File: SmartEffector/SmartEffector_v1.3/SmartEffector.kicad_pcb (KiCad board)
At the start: 2 copper layers, 83.2 x 72.1 mm, 53 parts, among them M1 FID, M10 M_2.9mm, M11 M_2.9mm, M13 Ziptie, M15 OSHW_Logo, M16 12mm, M2 FID, M3 M_2.9mm, M4 M_2.9mm, M5 M_2.9mm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

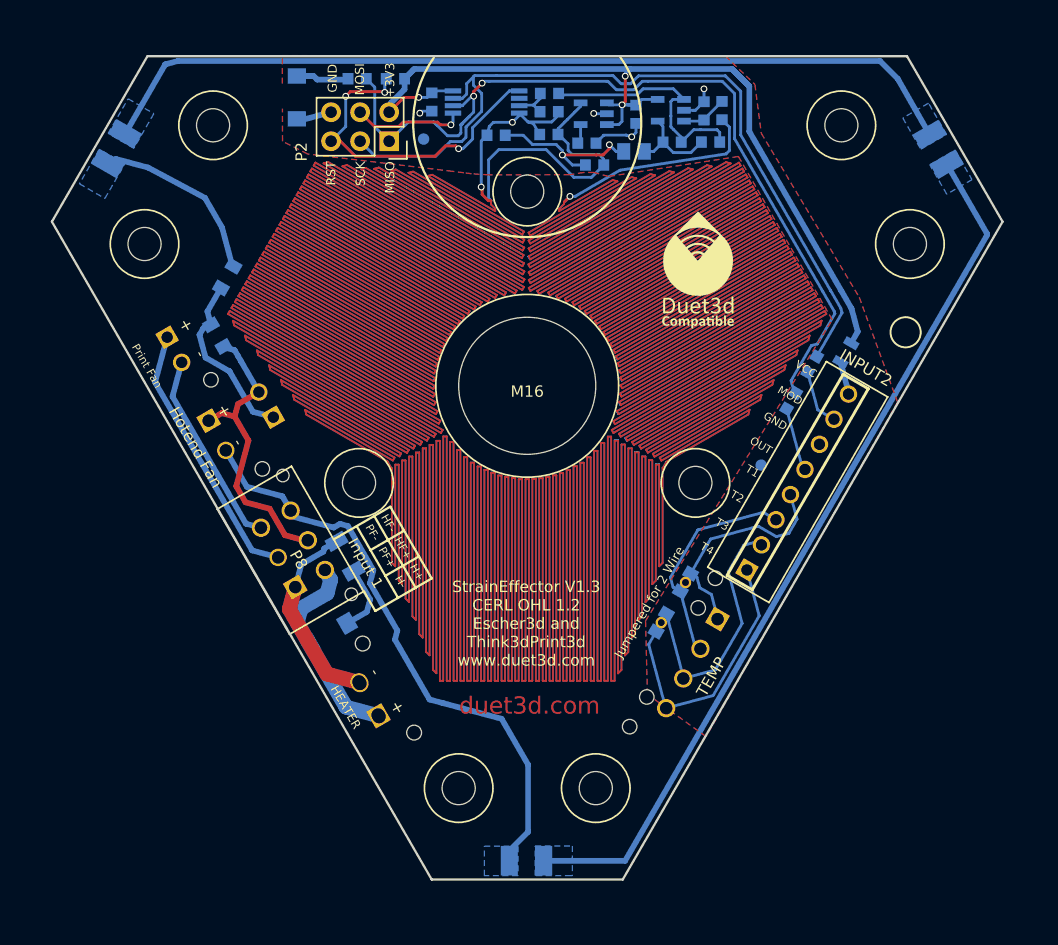
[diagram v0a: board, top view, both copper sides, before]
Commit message: Added modifications for puplomaker delta printer
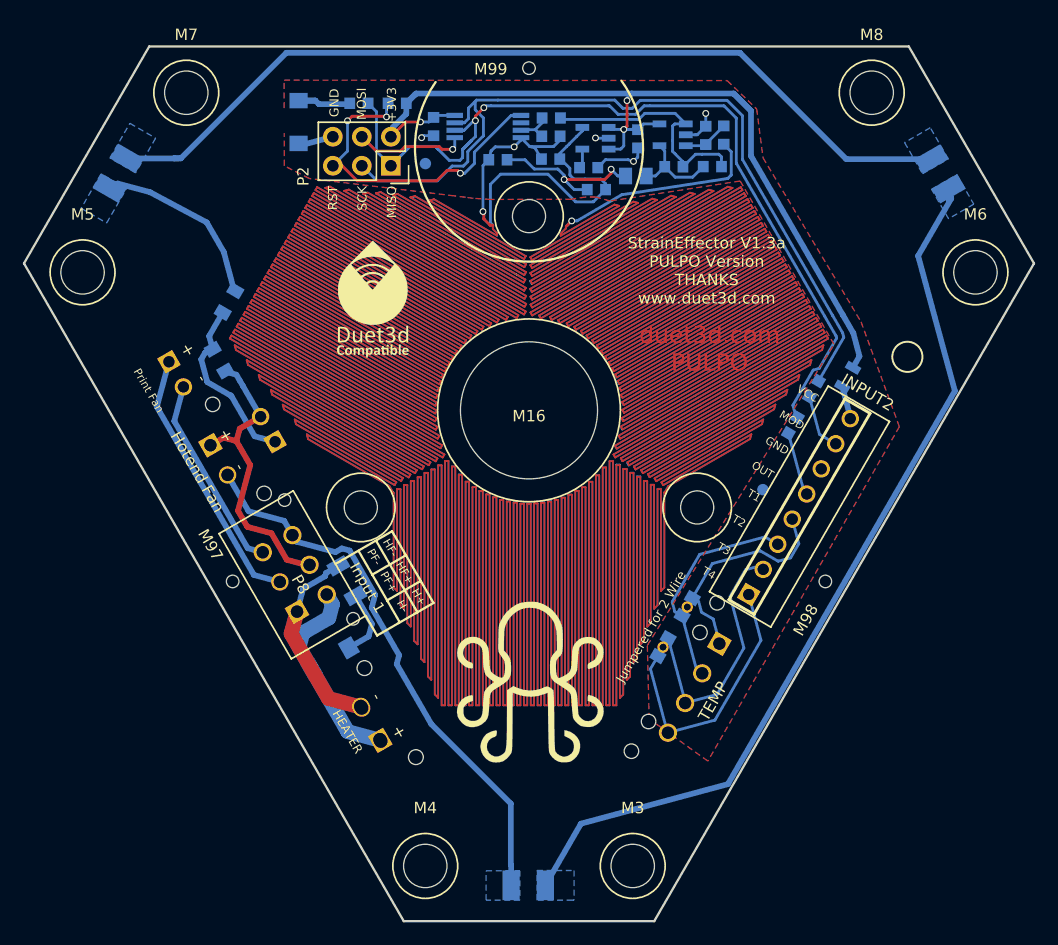
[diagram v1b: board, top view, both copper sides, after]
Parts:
- added G99: LOGO, Wire_Pads:LOGO, F.Cu at (84.2, 149.5)
- added M97: M2_1.4mm, Wire_Pads:M2_2.4, F.Cu at (58.2, 140.9)
- added M98: M2_1.4mm, Wire_Pads:M2_2.4, F.Cu at (110.1, 140.9)
- added M99: M2_1.4mm, Wire_Pads:M2_2.4, F.Cu at (84.2, 96.0)
- M3, M4, M5, M6, M7, M8: value M_2.9mm -> M_3.8mm; footprint complib:MountingHole_2.9mm -> Wire_Pads:M4_3.8
- moved M15 28.6 mm to (70.5, 116.1)
- moved M3 7.54 mm to (93.3, 165.8)
- moved M4 7.41 mm to (75.1, 165.8)
- moved M6 6.25 mm to (123.3, 113.8)
- moved M5 5.97 mm to (45.1, 113.8)
- moved M8 3.90 mm to (114.2, 98.1)
- moved M7 3.69 mm to (54.2, 98.1)
- moved D3 2.15 mm to (64.0, 100.7)
- moved M13 2.15 mm to (117.3, 121.2)
- moved P9 2.15 mm to (57.1, 130.3)
- moved C8 2.15 mm to (99.7, 101.8)
- moved R1 2.15 mm to (100.2, 104.6)
- moved R7 2.15 mm to (72.6, 99.0)
- moved R14 2.15 mm to (81.5, 104.0)
- moved JP3 2.15 mm to (61.3, 127.6)
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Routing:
- net H_Fan_-: track 51.5 -> 49.1 mm
- net Net-(D7-Pad2): track 77.2 -> 79.2 mm
- net Net-(D1-Pad1): track 77.1 -> 78.5 mm
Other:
- board size 83.2 x 72.1 mm -> 88.4 x 76.6 mm
- board text added: "StrainEffector V1.3a PULPO Version THANKS www.duet3d.com"
- board text added: "duet3d.com PULPO"
- board text removed: "StrainEffector V1.3 CERL OHL 1.2 Escher3d and Think3dPrint3d www.duet3d.com"
- board text removed: "duet3d.com"

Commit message: charlio modification, gerbers and autogenerated BOM list
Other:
- board size 88.4 x 76.6 mm -> 86.9 x 76.6 mm
- board text added: "Based on StrainEffector V1.3a www.duet3d.com Pulpomaker Version"
- board text added: "David Carlos Sergio Santi Raúl Xavi Oriol Victor Javier"
- board text added: "Jumpered for 2 wire"
- board text removed: "Jumpered for 2 Wire"
- board text removed: "StrainEffector V1.3a PULPO Version THANKS www.duet3d.com"
- board text removed: "duet3d.com PULPO"
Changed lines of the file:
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@@
-(kicad_pcb (version 20171130) (host pcbnew 5.0.0+dfsg1-2)
+(kicad_pcb (version 20171130) (host pcbnew "(5.0.0)")
   (general
     (thickness 1.6)
-    (drawings 77)
+    (drawings 82)
     (tracks 1429)
     (zones 0)
@@
     (0 F.Cu signal)
     (31 B.Cu signal)
-    (32 B.Adhes user)
-    (33 F.Adhes user)
-    (34 B.Paste user)
-    (35 F.Paste user)
+    (32 B.Adhes user hide)
+    (33 F.Adhes user hide)
+    (34 B.Paste user hide)
+    (35 F.Paste user hide)
     (36 B.SilkS user)
     (37 F.SilkS user)
     (38 B.Mask user)
     (39 F.Mask user)
-    (40 Dwgs.User user)
-    (41 Cmts.User user)
-    (42 Eco1.User user)
-    (43 Eco2.User user)
+    (40 Dwgs.User user hide)
+    (41 Cmts.User user hide)
+    (42 Eco1.User user hide)
+    (43 Eco2.User user hide)
     (44 Edge.Cuts user)
-    (45 Margin user)
-    (46 B.CrtYd user)
-    (47 F.CrtYd user)
-    (48 B.Fab user)
-    (49 F.Fab user)
+    (45 Margin user hide)
+    (46 B.CrtYd user hide)
+    (47 F.CrtYd user hide)
+    (48 B.Fab user hide)
+    (49 F.Fab user hide)
   )
   (setup
@@
   (module Wire_Pads:M4_3.8 locked (layer F.Cu)
     (at 45.106803 113.838022)
-    (fp_text reference M5 (at 0 -5.08) (layer F.SilkS)
+    (fp_text reference M5 (at 0 -5.08) (layer F.SilkS) hide
       (effects (font (size 1 1) (thickness 0.15)))
     )
@@
   (module Wire_Pads:M4_3.8 locked (layer F.Cu)
     (at 54.186944 98.110756)
-    (fp_text reference M7 (at 0 -5.08) (layer F.SilkS)
+    (fp_text reference M7 (at 4.302525 -2.218279) (layer F.SilkS) hide
       (effects (font (size 1 1) (thickness 0.15)))
     )
@@
   (module Wire_Pads:M4_3.8 (layer F.Cu)
     (at 114.186946 98.110757)
-    (fp_text reference M8 (at 0 -5.08) (layer F.SilkS)
+    (fp_text reference M8 (at -3.881477 -1.83728) (layer F.SilkS) hide
       (effects (font (size 1 1) (thickness 0.15)))
     )
@@
   (module Wire_Pads:M4_3.8 locked (layer F.Cu)
     (at 123.267079 113.83802)
-    (fp_text reference M6 (at 0 -5.08) (layer F.SilkS)
+    (fp_text reference M6 (at 1.38939 -3.721543) (layer F.SilkS) hide
       (effects (font (size 1 1) (thickness 0.15)))
     )
@@
   (module Wire_Pads:M4_3.8 locked (layer F.Cu)
     (at 93.267087 165.799547)
-    (fp_text reference M3 (at 0 -5.08) (layer F.SilkS)
+    (fp_text reference M3 (at 0 -5.08) (layer F.SilkS) hide
       (effects (font (size 1 1) (thickness 0.15)))
     )
@@
   (module Wire_Pads:M4_3.8 locked (layer F.Cu)
     (at 75.106796 165.799547)
-    (fp_text reference M4 (at 0 -5.08) (layer F.SilkS)
+    (fp_text reference M4 (at 0 -5.08) (layer F.SilkS) hide
       (effects (font (size 1 1) (thickness 0.15)))
     )
@@
   (module Wire_Pads:M2_2.4 (layer F.Cu)
     (at 84.186943 95.960759)
-    (fp_text reference M99 (at -3.348806 0.084343) (layer F.SilkS)
+    (fp_text reference M99 (at -3.348806 0.084343) (layer F.SilkS) hide
       (effects (font (size 1 1) (thickness 0.15)))
     )
@@
   (module Wire_Pads:M2_2.4 (layer F.Cu)
     (at 58.244843 140.893787 120)
-    (fp_text reference M97 (at 3.736499 -0.083013 120) (layer F.SilkS)
+    (fp_text reference M97 (at 3.736499 -0.083013 120) (layer F.SilkS) hide
       (effects (font (size 1 1) (thickness 0.15)))
     )
@@
   (module Wire_Pads:M2_2.4 (layer F.Cu)
     (at 110.129047 140.893789 240)
-    (fp_text reference M98 (at 3.777945 -0.201285 240) (layer F.SilkS)
+    (fp_text reference M98 (at 3.777945 -0.201285 240) (layer F.SilkS) hide
       (effects (font (size 1 1) (thickness 0.15)))
     )
@@
       (effects (font (size 1 1) (thickness 0.15)) (justify mirror))
     )
-    (fp_text user K (at -3.957066 0.991181 240) (layer B.SilkS)
+    (fp_text user K (at -3.957066 0.991181 240) (layer B.SilkS) hide
       (effects (font (size 0.9 0.9) (thickness 0.1)) (justify mirror))
     )
@@
       (effects (font (size 1 1) (thickness 0.15)) (justify mirror))
     )
-    (fp_text user K (at -4.102768 0.812217) (layer B.SilkS)
+    (fp_text user K (at -4.102768 0.812217) (layer B.SilkS) hide
       (effects (font (size 0.9 0.9) (thickness 0.1)) (justify mirror))
     )
@@
       (effects (font (size 1 1) (thickness 0.15)) (justify mirror))
     )
-    (fp_text user K (at -3.41469 0.797969 120) (layer B.SilkS)
+    (fp_text user K (at -3.41469 0.797969 120) (layer B.SilkS) hide
       (effects (font (size 0.9 0.9) (thickness 0.1)) (justify mirror))
     )
@@
       (xy -1.056581 0.682429)) (layer F.SilkS) (width 0.01))
   )
+  (gr_line (start 126.959844 115.486448) (end 96.601596 168.068477) (layer Edge.Cuts) (width 0.2))
+  (gr_arc (start 53.839971 99.003171) (end 53.839971 94.003171) (angle -60) (layer Edge.Cuts) (width 0.2))
+  (gr_arc (start 45.766723 112.986448) (end 41.436596 110.486448) (angle -60) (layer Edge.Cuts) (width 0.2))
+  (gr_line (start 53.839971 94.003171) (end 114.556469 94.003171) (layer Edge.Cuts) (width 0.2))
+  (gr_arc (start 114.556469 99.003171) (end 118.886596 96.503171) (angle -60) (layer Edge.Cuts) (width 0.2))
+  (gr_line (start 118.886596 96.503171) (end 126.959844 110.486448) (layer Edge.Cuts) (width 0.2))
+  (gr_arc (start 122.629717 112.986448) (end 126.959844 115.486448) (angle -60) (layer Edge.Cuts) (width 0.2))
+  (gr_arc (start 92.271469 165.568477) (end 92.271469 170.568477) (angle -60) (layer Edge.Cuts) (width 0.2))
+  (gr_arc (start 76.124971 165.568477) (end 71.794844 168.068477) (angle -60) (layer Edge.Cuts) (width 0.2))
+  (gr_line (start 71.794844 168.068477) (end 41.436596 115.486448) (layer Edge.Cuts) (width 0.2))
+  (gr_line (start 41.436596 110.486448) (end 49.509844 96.503171) (layer Edge.Cuts) (width 0.2))
+  (gr_line (start 92.271469 170.568477) (end 76.124971 170.568477) (layer Edge.Cuts) (width 0.2))
   (gr_text T2 (at 102.562039 135.614841 -30) (layer F.SilkS)
     (effects (font (size 0.7 0.7) (thickness 0.08)))
@@
   )
   (gr_arc (start 84.186942 102.916111) (end 92.272014 97.055601) (angle 251) (layer F.SilkS) (width 0.2))
-  (gr_text "Jumpered for 2 Wire" (at 94.875525 144.858812 60) (layer F.SilkS)
+  (gr_text "Jumpered for 2 wire" (at 95.192469 144.533477 60) (layer F.SilkS)
     (effects (font (size 0.8 0.8) (thickness 0.1)))
   )
@@
     (effects (font (size 0.8 0.8) (thickness 0.1)) (justify right))
   )
-  (gr_text "duet3d.com\nPULPO" (at 99.994702 120.529389) (layer F.Mask)
-    (effects (font (size 1.5 1.5) (thickness 0.26)))
-  )
-  (gr_text "duet3d.com\nPULPO" (at 99.997469 120.530477) (layer F.Cu)
-    (effects (font (size 1.5 1.5) (thickness 0.3)))
+  (gr_text "David\nCarlos\nSergio\nSanti\nRaúl\nXavi\nOriol\nVictor\nJavier" (at 98.367469 118.879477) (layer Dwgs.User)
+    (effects (font (size 1.5 1.5) (thickness 0.26)) (justify mirror))
   )
   (gr_text "RST\n\nSCK\n\nMISO" (at 69.593453 106.259225 90) (layer F.SilkS)
@@
     (effects (font (size 1 1) (thickness 0.1)))
   )
-  (gr_text "StrainEffector V1.3a\nPULPO Version\nTHANKS\nwww.duet3d.com" (at 99.744701 113.68939) (layer F.SilkS)
+  (gr_text "Based on\nStrainEffector V1.3a\nwww.duet3d.com\n\nPulpomaker Version\n" (at 101.288469 115.704477) (layer F.SilkS)
     (effects (font (size 1 1) (thickness 0.2)))
   )
-  (gr_line (start 39.979186 113.049393) (end 73.225969 170.634506) (angle 90) (layer Edge.Cuts) (width 0.2))
-  (gr_line (start 50.940158 94.064428) (end 39.979183 113.049396) (angle 90) (layer Edge.Cuts) (width 0.2))
-  (gr_line (start 117.433727 94.064431) (end 50.940159 94.064432) (angle 90) (layer Edge.Cuts) (width 0.2))
-  (gr_line (start 128.394701 113.04939) (end 117.433728 94.064424) (angle 90) (layer Edge.Cuts) (width 0.2))
-  (gr_line (start 95.14792 170.634512) (end 128.394704 113.049389) (angle 90) (layer Edge.Cuts) (width 0.2))
-  (gr_line (start 95.14792 170.634512) (end 73.225967 170.634514) (angle 90) (layer Edge.Cuts) (width 0.2))
   (segment (start 72.096943 101.966108) (end 72.096943 101.601112) (width 0.5) (layer B.Cu) (net 1))
   (segment (start 112.534436 122.190205) (end 113.118868 121.177945) (width 0.5) (layer B.Cu) (net 1))
